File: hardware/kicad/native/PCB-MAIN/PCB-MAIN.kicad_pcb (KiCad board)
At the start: 6 copper layers, 110 x 75 mm, 251 parts, among them J10 U.FL-R-SMT-1(60), J11 USB4105-GF-A-120, J12 MEM2052-00-195-00-A, J13 504050-0291, J6 2336582-1, J7 2336582-1, J8 U.FL-R-SMT-1(60), J9 U.FL-R-SMT-1(60), Q1 MMBT3904,215, Q2 MMBT3904,215, Q3 MMBT3904,215, Q4 Si1016X-T1-GE3, U1 STM32U585VIT6Q, U10 E22-900M22S, U11 MDBT50Q-P1MV2, U13 TS3A27518EPWR, U14 ESDALC6V1-5P6, U15 ESDALC6V1-5P6, U16 SN74AXC8T245PWR, U17 SN74LVC32APWR, U18 SN74AXC1T45DRLR, U19 TPD4E05U06DQAR, U2 W25Q512JVFIQ, U20 TPD4E05U06DQAR, U21 TPD4E05U06DQAR, U22 TPD4E05U06DQAR, U23 TPD4E05U06DQAR, U24 TPD4E05U06DQAR, U25 TPD2EUSB30DRTR, U26 TPD2EUSB30DRTR, U27 TPD4E05U06DQAR, U3 LIS2DW12TR, U4 STTS22HTR, U5 LT6000IDCB#TRMPBF, U6 SN74LVC1G07DBVR, U7 SN74AXC8T245PWR, U8 BG95-M3, U9 MAX-M10S-00B, X1 SiT1552AI-JE-DCC-32.768D

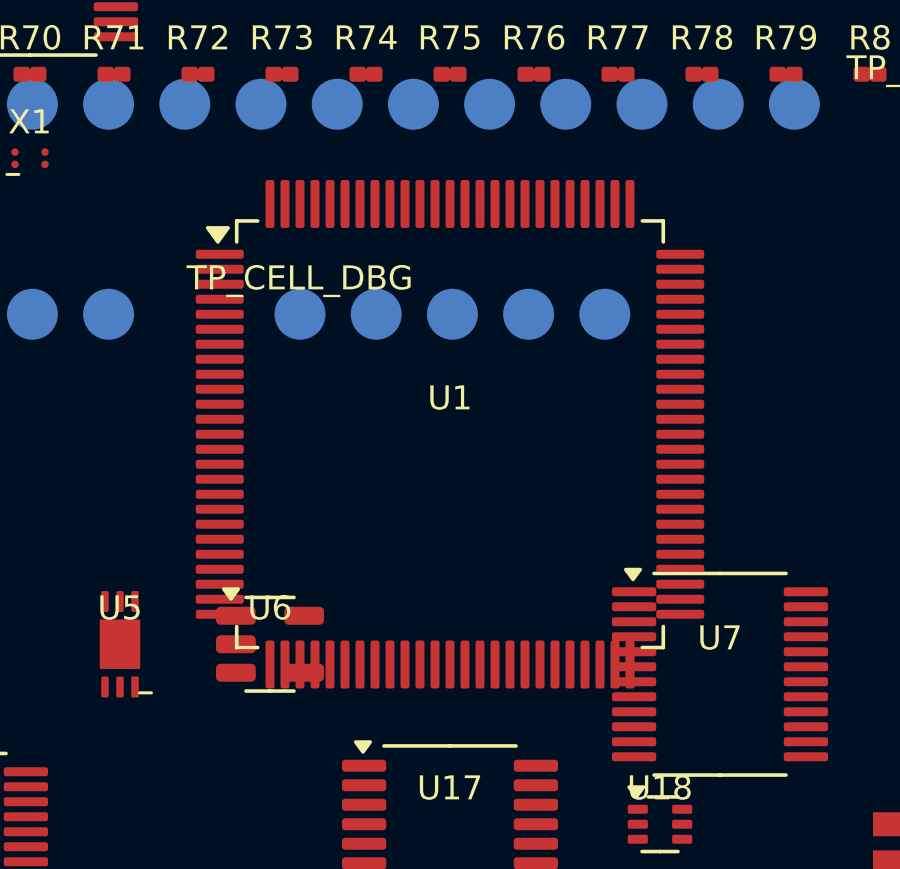
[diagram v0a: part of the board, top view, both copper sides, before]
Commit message: pcb(main): control STM32U585 LQFP100 footprint
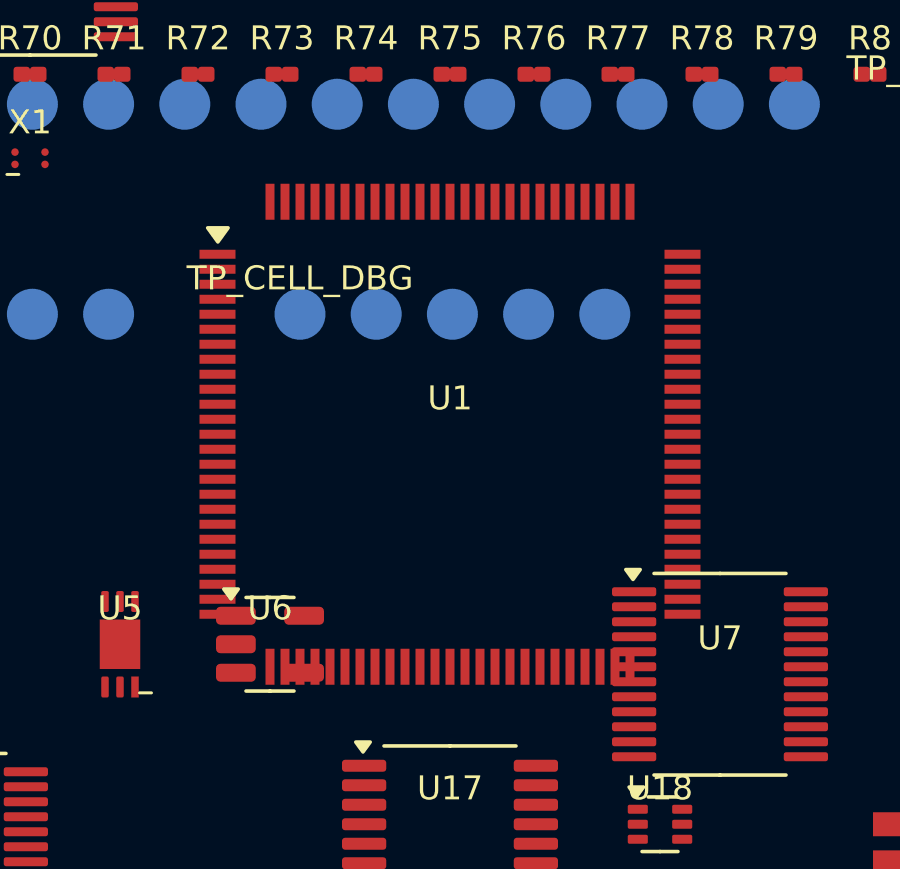
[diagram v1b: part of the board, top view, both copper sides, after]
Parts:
- U1: footprint LQFP-100_14x14mm_P0.5mm -> ST_STM32U585_LQFP100_1L

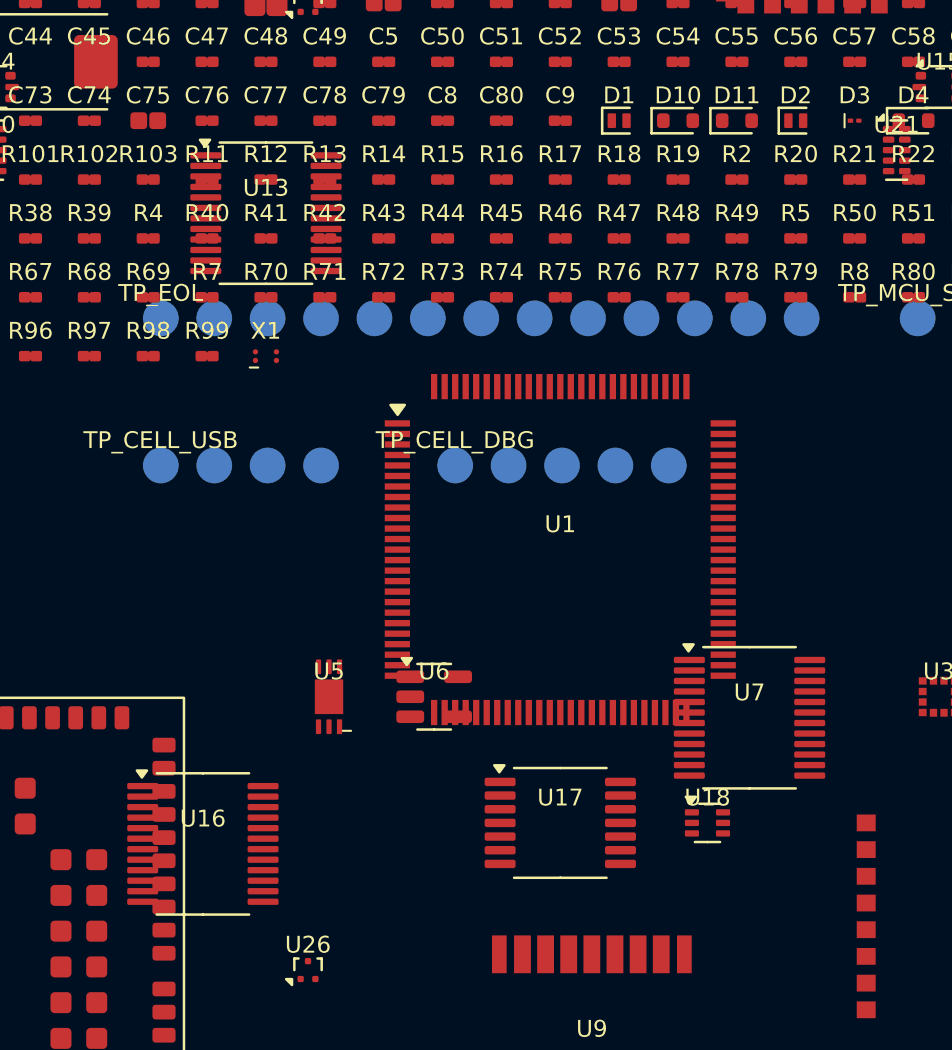
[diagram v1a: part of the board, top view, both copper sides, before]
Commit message: pcb(main): correct TI PW TSSOP land patterns
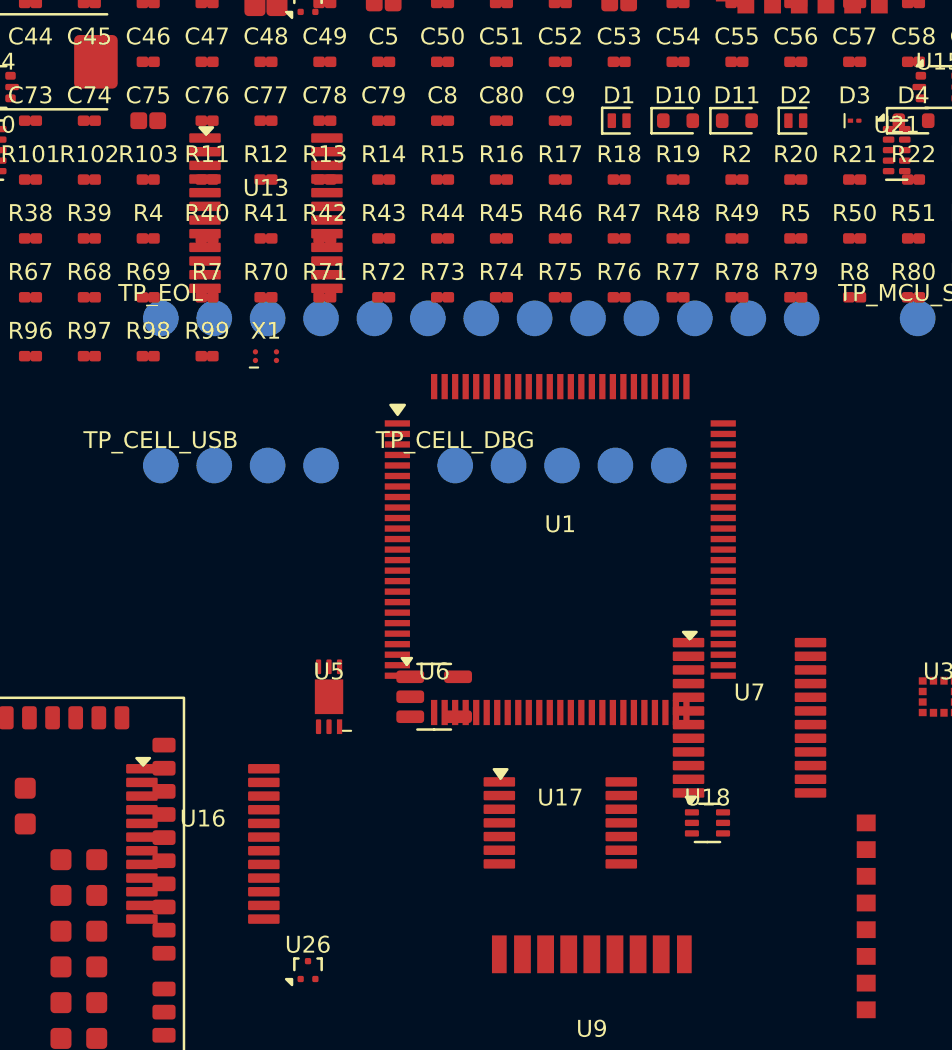
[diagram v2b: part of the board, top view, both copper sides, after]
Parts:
- U13, U16, U7: footprint TSSOP-24_4.4x6.5mm_P0.5mm -> TI_PW0024A_TSSOP24
- U17: footprint TSSOP-14_4.4x5mm_P0.65mm -> TI_PW0014A_TSSOP14

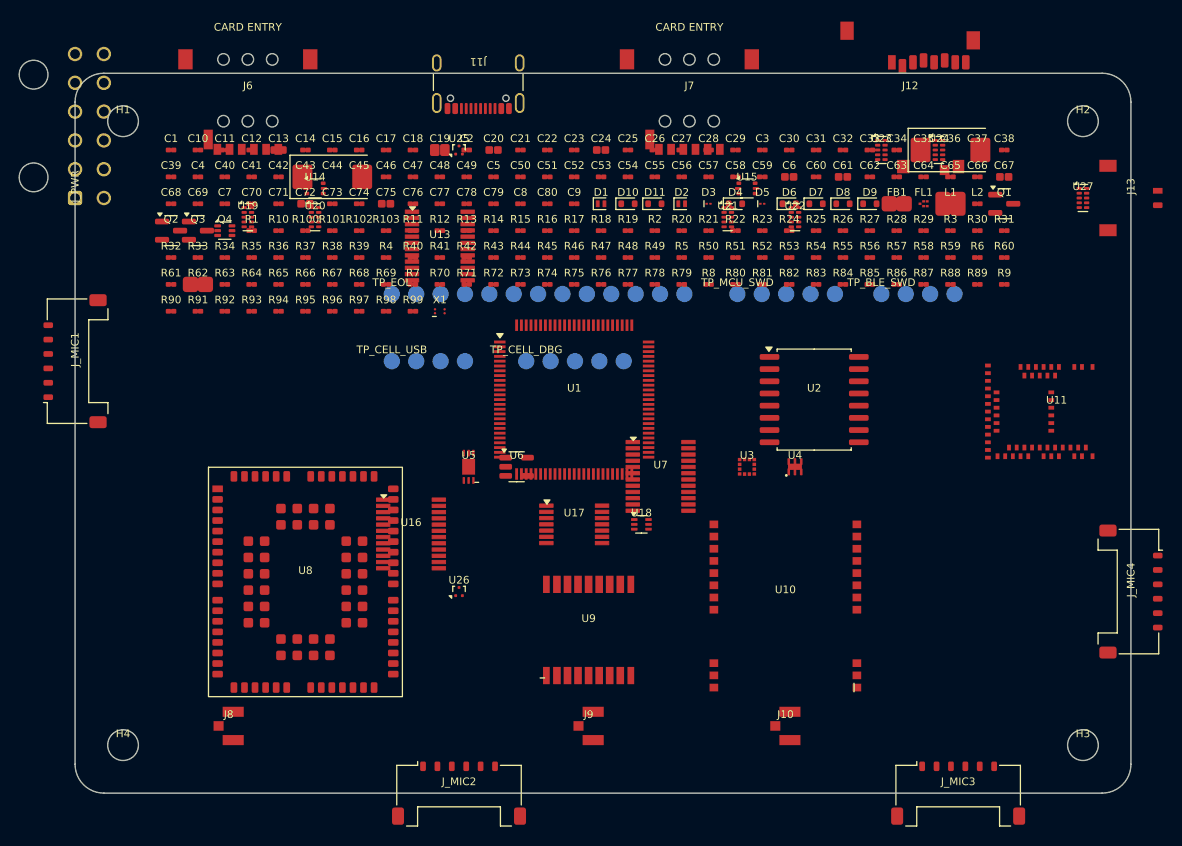
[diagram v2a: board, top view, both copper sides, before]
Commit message: pcb(main): control TI DRL and DQA land patterns
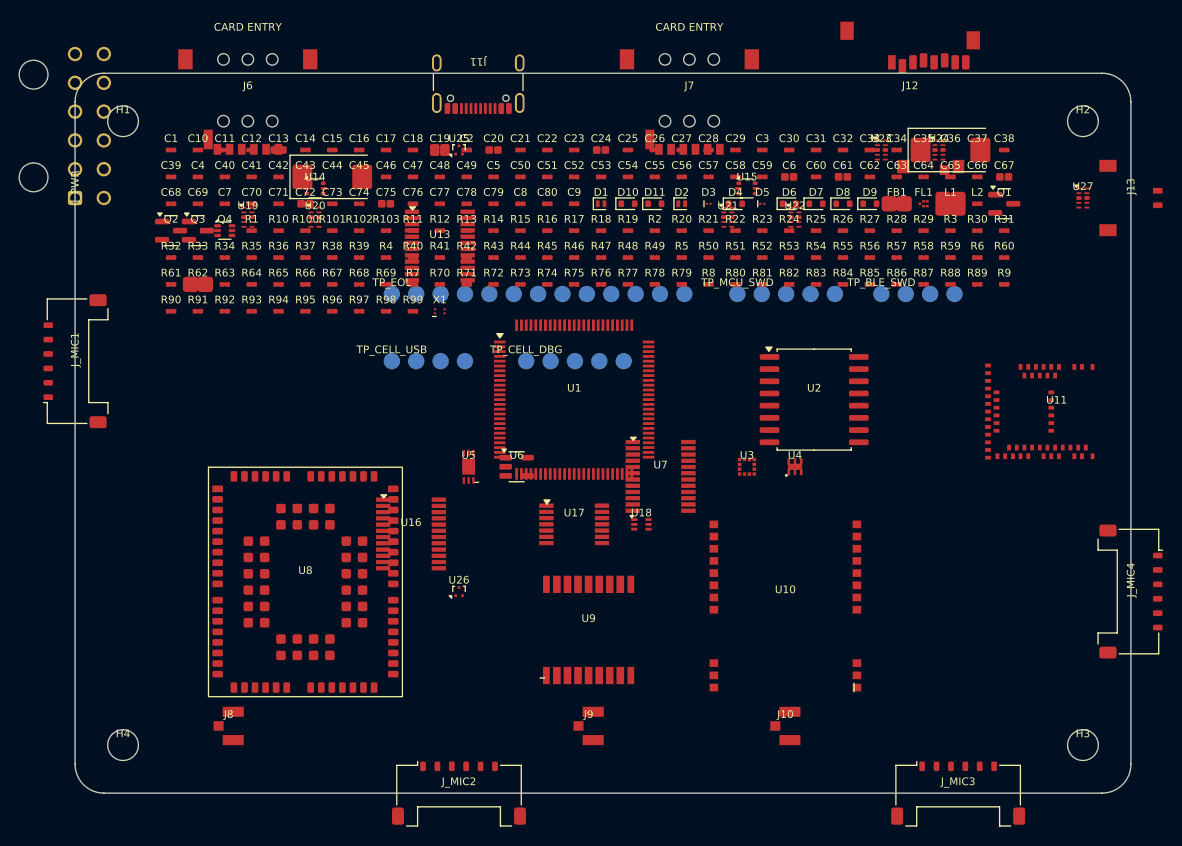
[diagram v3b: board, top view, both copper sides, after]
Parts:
- U18: footprint Texas_R-PDSO-N6_DRL-6 -> TI_DRL0006A_SOT6
- U19, U20, U21, U22, U23, U24, U27: footprint USON-10_2.5x1.0mm_P0.5mm -> TI_DQA0010A_USON10

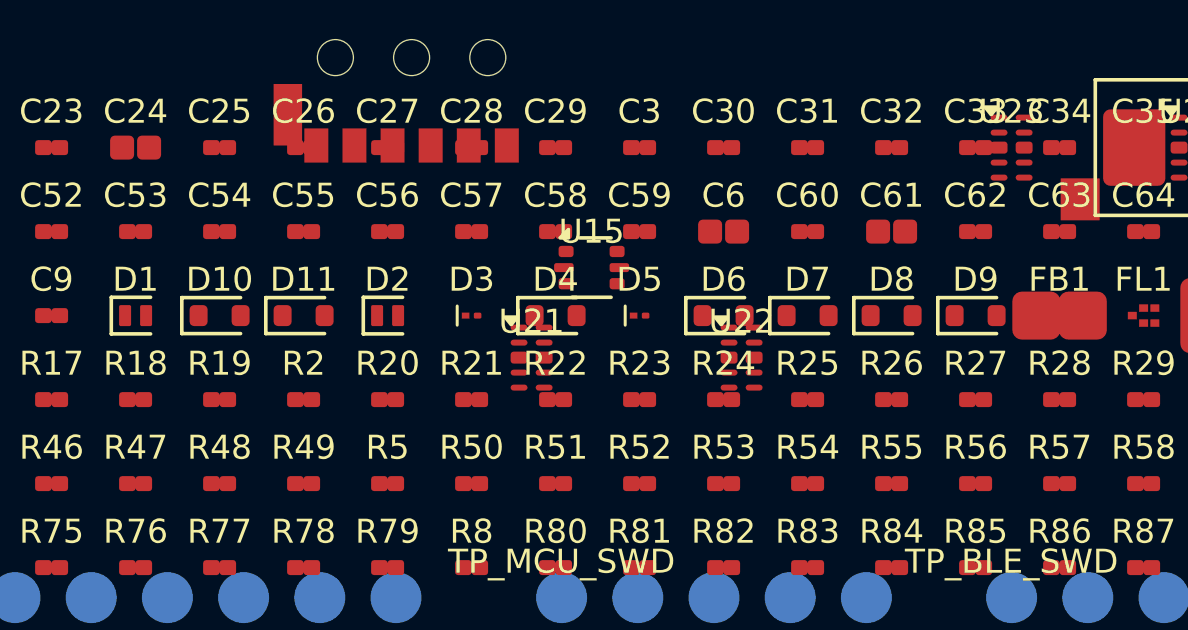
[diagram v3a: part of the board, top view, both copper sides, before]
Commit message: pcb(main): control TI DYA SOD-523 land pattern
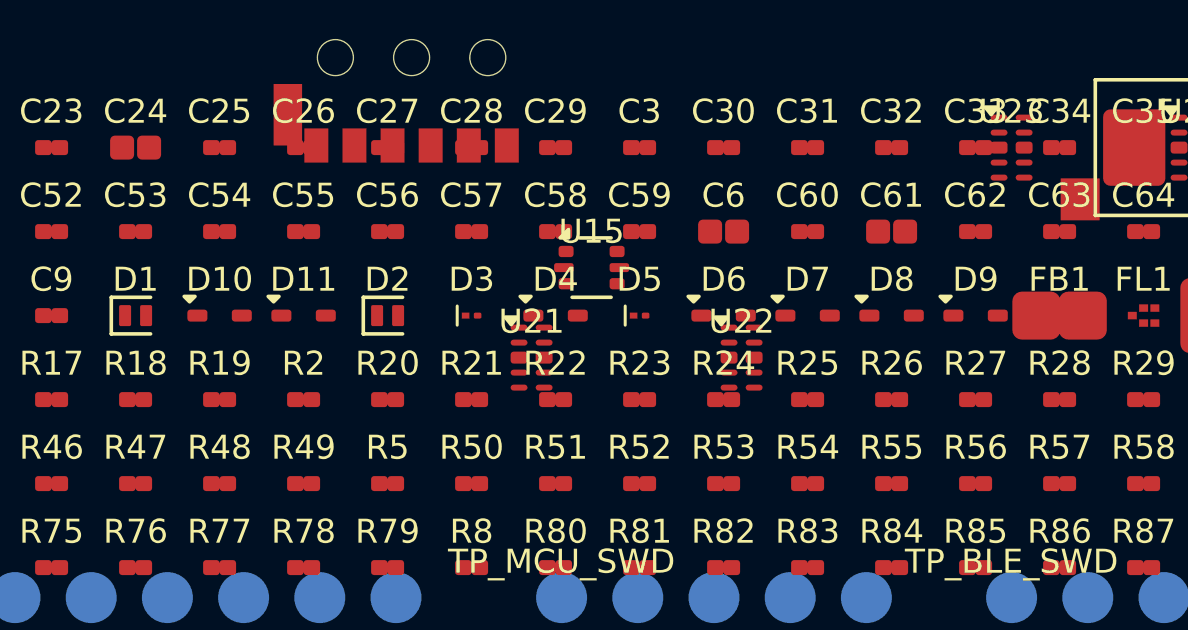
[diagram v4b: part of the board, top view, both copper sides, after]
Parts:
- D10, D11, D4, D6, D7, D8, D9: footprint D_SOD-523 -> TI_DYA0002A_SOD523

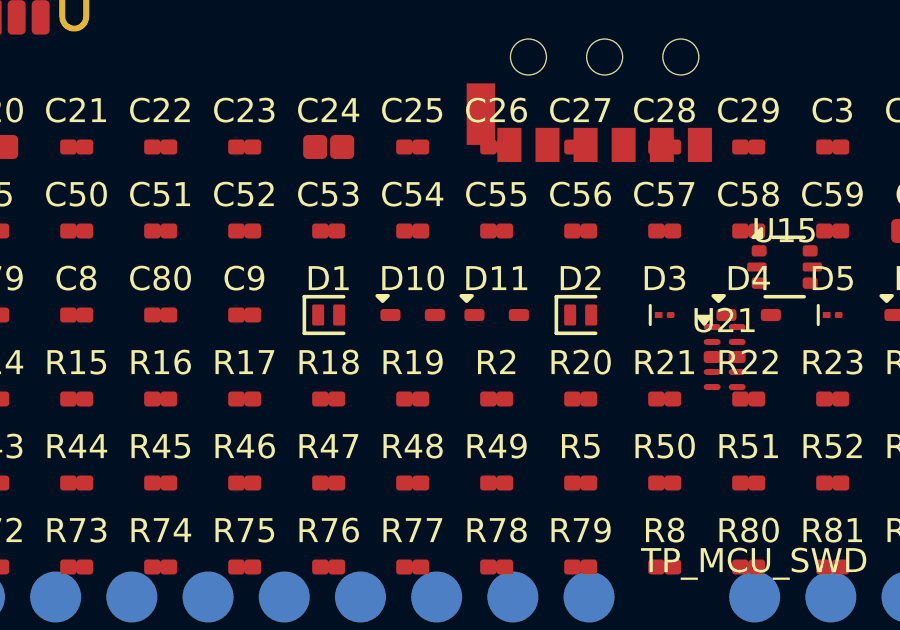
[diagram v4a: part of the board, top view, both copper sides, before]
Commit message: pcb(main): control Nexperia SOD882 land pattern
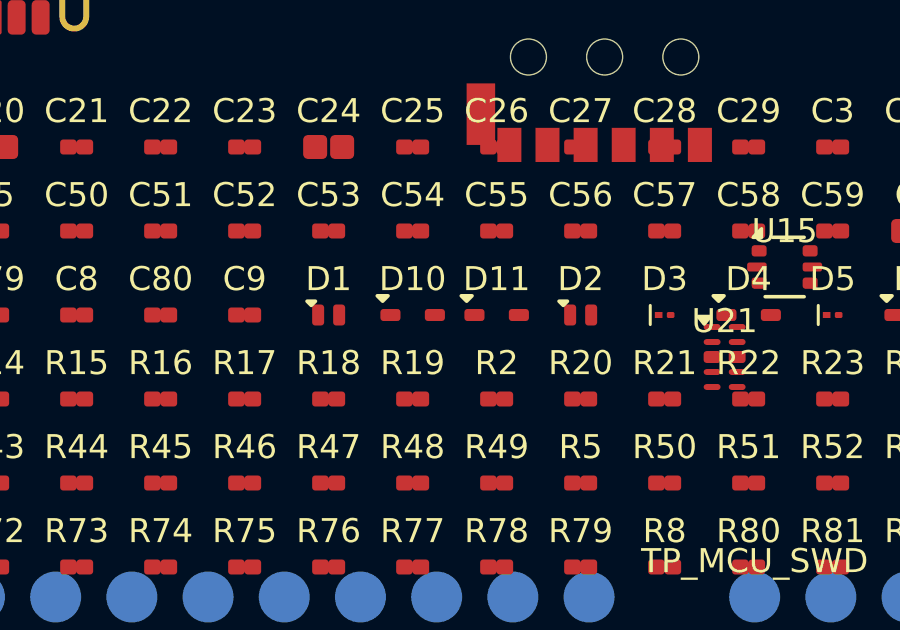
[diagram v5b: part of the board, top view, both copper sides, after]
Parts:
- D1, D2: footprint D_SOD-882 -> Nexperia_PESD5V0S1UL_SOD882

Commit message: pcb(main): control Nexperia SOT23 land pattern
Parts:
- Q1, Q2, Q3: footprint SOT-23 -> Nexperia_MMBT3904_SOT23
